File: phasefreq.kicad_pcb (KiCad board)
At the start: 4 copper layers, 90.5 x 56 mm, 109 parts, among them J1 Power Input, J2 RF Input, J3 LO Input, J4 VCO Tune, U1 LM317_3PinPackage, U2 LM337_SOT223, U3 ADCMP564, U4 AD9901, U5 LM4040DIZ-2.5, U6 AD8676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

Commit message: missing trace fixed, drc now passes
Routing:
- net VCC: track 146.0 -> 149.5 mm

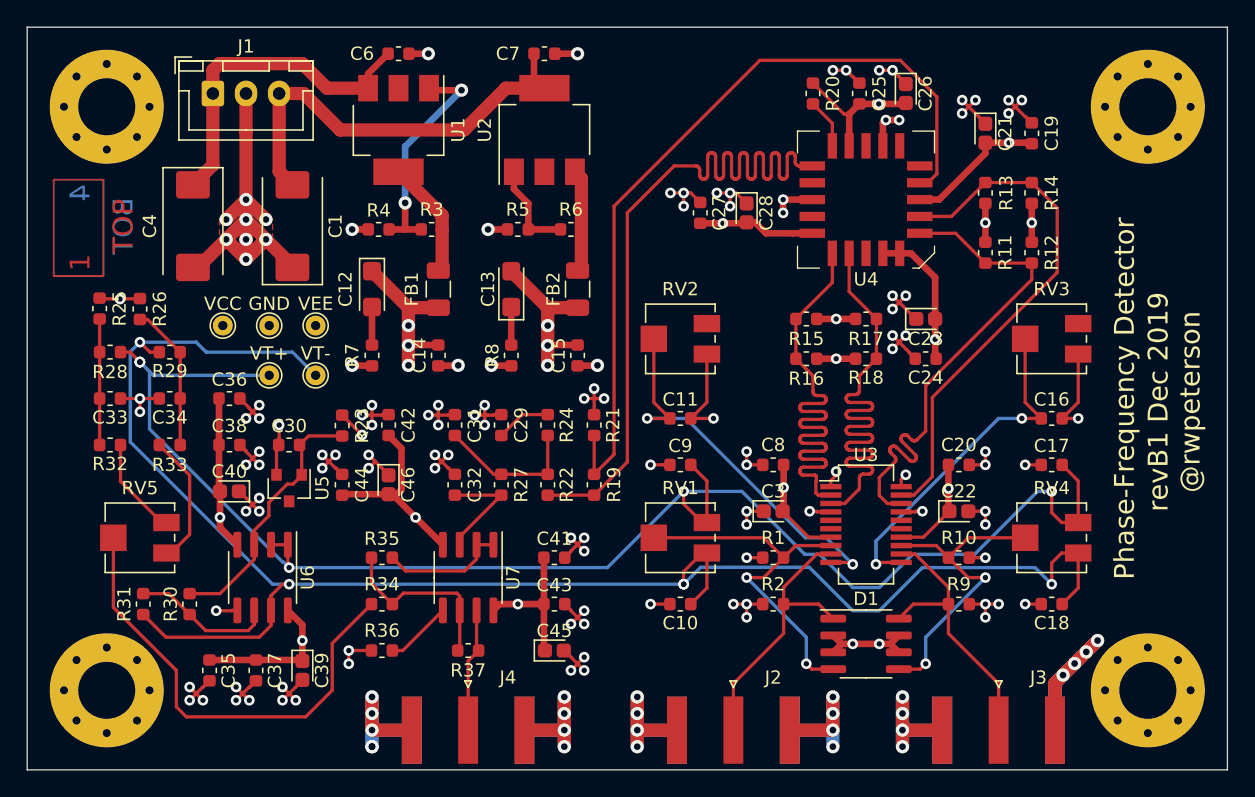
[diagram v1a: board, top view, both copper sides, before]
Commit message: added mounting holes and test points to sch, added ferrite beads to op amp supplies
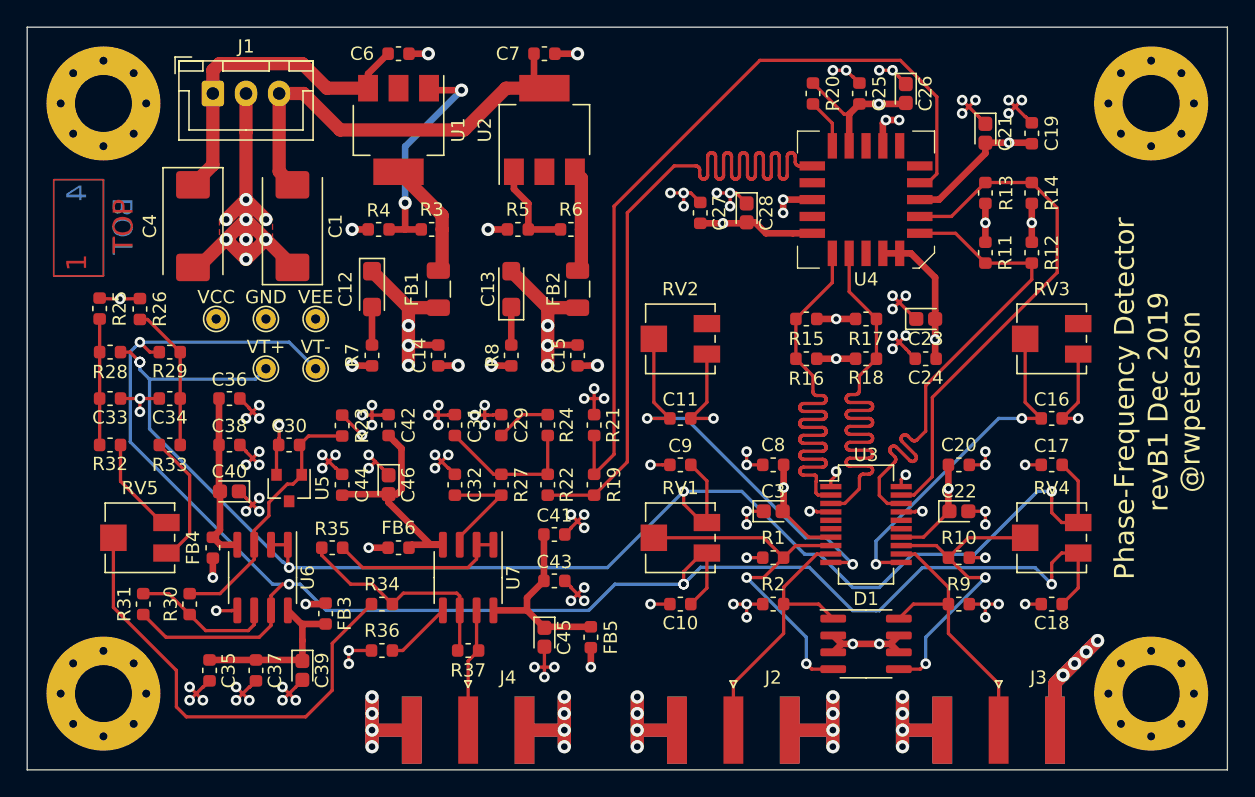
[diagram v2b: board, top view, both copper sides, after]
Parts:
- removed REF** (x4): MountingHole_4.3mm_M4_Pad_Via, MountingHole:MountingHole_4.3mm_M4_Pad_Via
- added FB3: BLM18PG221SZ1D, Inductor_SMD:L_0603_1608Metric, F.Cu at (144.8, 124.2)
- added FB4: BLM18PG221SZ1D, Inductor_SMD:L_0603_1608Metric, F.Cu at (136.2, 119.2)
- added FB5: BLM18PG221SZ1D, Inductor_SMD:L_0603_1608Metric, F.Cu at (164.8, 126.0)
- added FB6: BLM18PG221SZ1D, Inductor_SMD:L_0603_1608Metric, F.Cu at (150.2, 119.2)
- added H1: M4, MountingHole:MountingHole_4.3mm_M4_Pad_Via, F.Cu at (128.0, 85.8)
- added H2: M4, MountingHole:MountingHole_4.3mm_M4_Pad_Via, F.Cu at (128.0, 130.2)
- added H3: M4, MountingHole:MountingHole_4.3mm_M4_Pad_Via, F.Cu at (207.0, 85.8)
- added H4: M4, MountingHole:MountingHole_4.3mm_M4_Pad_Via, F.Cu at (207.0, 130.2)
- GND: value TestPoint_THTPad_D1.5mm_Drill0.7mm -> GND
- VCC: value TestPoint_THTPad_D1.5mm_Drill0.7mm -> VCC
- VEE: value TestPoint_THTPad_D1.5mm_Drill0.7mm -> VEE
- VT+: value TestPoint_THTPad_D1.5mm_Drill0.7mm -> VT+
- VT-: value TestPoint_THTPad_D1.5mm_Drill0.7mm -> VT-
- moved R35 3.82 mm to (145.2, 119.2)
- moved C41 1.75 mm to (162.0, 118.2)
- moved C43 1.75 mm to (162.0, 121.8)
- moved C45 1.25 mm to (161.2, 126.0), turned to 270 degrees
- moved VCC 0.71 mm to (136.5, 102.0)
- moved GND 0.56 mm to (140.2, 102.0)
- moved VT+ 0.56 mm to (140.2, 105.8)
- moved VEE 0.50 mm to (144.0, 102.0)
- moved VT- 0.50 mm to (144.0, 105.8)
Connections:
- C35 pad 1: VCC -> Net-(C35-Pad1)
- C36 pad 1: VEE -> Net-(C36-Pad1)
- C37 pad 1: VCC -> Net-(C35-Pad1)
- C38 pad 1: VEE -> Net-(C36-Pad1)
- C39 pad 1: VCC -> Net-(C35-Pad1)
- C40 pad 2: VEE -> Net-(C36-Pad1)
- C41 pad 1: VCC -> Net-(C41-Pad1)
- C42 pad 1: VEE -> Net-(C42-Pad1)
- C43 pad 1: VCC -> Net-(C41-Pad1)
- C44 pad 1: VEE -> Net-(C42-Pad1)
- C45 pad 1: VCC -> Net-(C41-Pad1)
- C46 pad 2: VEE -> Net-(C42-Pad1)
- U6 pad 4: VEE -> Net-(C36-Pad1)
- U6 pad 8: VCC -> Net-(C35-Pad1)
- U7 pad 4: VEE -> Net-(C42-Pad1)
- U7 pad 8: VCC -> Net-(C41-Pad1)
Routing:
- net Net-(C42-Pad1): track 0.00 -> 17.7 mm
- net VCC: track 149.5 -> 133.0 mm
- net Net-(C41-Pad1): track 0.00 -> 14.2 mm
- net Net-(C35-Pad1): track 0.00 -> 13.1 mm
- net Net-(C36-Pad1): track 0.00 -> 12.8 mm
- net Net-(R35-Pad2): track 9.48 -> 13.3 mm
- net Net-(R34-Pad1): track 13.8 -> 17.1 mm
- net GNDA: track 285.5 -> 288.2 mm, vias 151 -> 150
- net VTUNE-: track 132.1 -> 133.6 mm
- net VEE: track 262.6 -> 263.8 mm
